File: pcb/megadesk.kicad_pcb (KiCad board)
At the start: 2 copper layers, 41.7 x 32.2 mm, 24 parts, among them J2 FFC, J3 AVR-ISP-6, J4 Interface, U1 7812, U2 HT7550-1, U3 ATtiny841-SS, U4 MCP2003B

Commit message: ignore update
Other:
- board text added: "BZ1 has no polarity"
- board text removed: "+"
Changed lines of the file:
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@@
   (gr_line (start 140.45 114.1) (end 97.7 114.1)
     (stroke (width 0.2) (type solid)) (layer "Dwgs.User"))
+  (gr_line (start 135.3 117.2) (end 133.7 118.8)
+    (stroke (width 0.3) (type default)) (layer "Cmts.User"))
+  (gr_line (start 133.7 118.8) (end 147.6 118.8)
+    (stroke (width 0.3) (type default)) (layer "Cmts.User"))
+  (gr_line (start 133.7 118.8) (end 135.3 120.4)
+    (stroke (width 0.3) (type default)) (layer "Cmts.User"))
+  (gr_line (start 133.7 118.8) (end 135.3 117.2)
+    (stroke (width 0.1) (type default)) (layer "Cmts.User"))
   (gr_line (start 121.336 70.940102) (end 121.336 117.892102)
     (stroke (width 0.15) (type solid)) (layer "Eco1.User"))
@@
     (effects (font (size 0.8 0.8) (thickness 0.125)))
   )
-  (gr_text "+" (at 129.7 118.8 270) (layer "F.SilkS")
-    (effects (font (size 1 1) (thickness 0.15)))
-  )
   (gr_text "RST\nGND" (at 115.4 118.9) (layer "F.SilkS")
     (effects (font (size 0.7 0.7) (thickness 0.1)) (justify right))
@@
     (effects (font (size 1 1) (thickness 0.15)))
   )
+  (gr_text "BZ1 has no polarity" (at 142.4 118.4) (layer "Cmts.User")
+    (effects (font (size 1 1) (thickness 0.15)) (justify left bottom))
+  )
   (segment (start 105.525 123) (end 107.625 125.1) (width 0.4) (layer "F.Cu") (net 1))

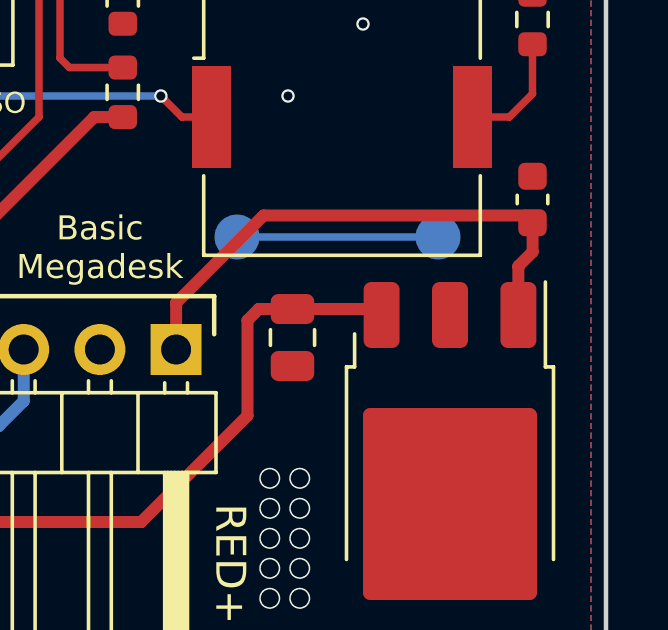
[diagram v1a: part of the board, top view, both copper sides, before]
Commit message: 2pin 7812
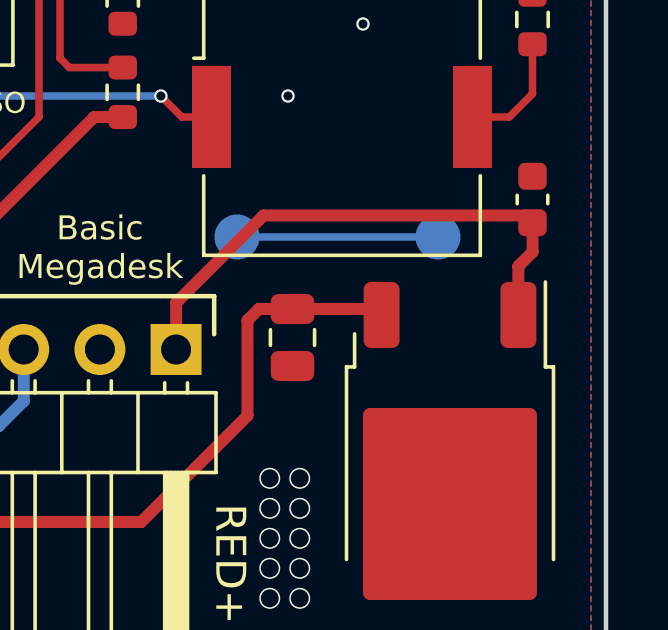
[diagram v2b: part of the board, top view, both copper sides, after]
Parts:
- U1: footprint Package_TO_SOT_SMD:TO-252-3_TabPin2 -> Package_TO_SOT_SMD:TO-252-2
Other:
- board text added: "megadesk v11a"
- board text removed: "megadesk v11"
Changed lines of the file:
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@@
     )
   )
-  (footprint "Package_TO_SOT_SMD:TO-252-3_TabPin2" (layer "F.Cu")
+  (footprint "Package_TO_SOT_SMD:TO-252-2" (layer "F.Cu")
     (at 135.7 130.44 -90)
     (descr "TO-252/DPAK SMD package, http://www.infineon.com/cms/en/product/packages/PG-TO252/PG-TO252-3-1/")
@@
     (property "ki_keywords" "Voltage Regulator 1.5A Positive")
     (attr smd)
-    (fp_text reference "U1" (at 0 -4.5 90) (layer "F.SilkS") hide
-        (effects (font (size 1 1) (thickness 0.15)))
-    )
-    (fp_text value "7812" (at 6.5 0.105 180) (layer "F.SilkS") hide
-        (effects (font (size 0.8 0.8) (thickness 0.13)))
-    )
-    (fp_text user "${REFERENCE}" (at 0 0 90) (layer "F.Fab")
+    (fp_text reference "U1" (at 0 -4.5 -90) (layer "F.SilkS") hide
+        (effects (font (size 1 1) (thickness 0.15)))
+    )
+    (fp_text value "7812" (at -4.24 -0.1 -90) (layer "F.Fab")
+        (effects (font (size 1 1) (thickness 0.15)))
+    )
+    (fp_text user "${REFERENCE}" (at 0 0 -90) (layer "F.Fab")
         (effects (font (size 1 1) (thickness 0.15)))
     )
@@
     (fp_line (start -5.81 -1.905) (end -3.11 -1.905)
       (stroke (width 0.1) (type solid)) (layer "F.Fab"))
-    (fp_line (start -5.81 -0.375) (end -5.81 0.375)
-      (stroke (width 0.1) (type solid)) (layer "F.Fab"))
-    (fp_line (start -5.81 0.375) (end -3.11 0.375)
-      (stroke (width 0.1) (type solid)) (layer "F.Fab"))
     (fp_line (start -5.81 1.905) (end -5.81 2.655)
       (stroke (width 0.1) (type solid)) (layer "F.Fab"))
@@
       (stroke (width 0.1) (type solid)) (layer "F.Fab"))
     (fp_line (start -3.11 -2.25) (end -2.11 -3.25)
-      (stroke (width 0.1) (type solid)) (layer "F.Fab"))
-    (fp_line (start -3.11 -0.375) (end -5.81 -0.375)
       (stroke (width 0.1) (type solid)) (layer "F.Fab"))
     (fp_line (start -3.11 1.905) (end -5.81 1.905)
@@
     (pad "1" smd roundrect (at -5.04 -2.28 270) (size 2.2 1.2) (layers "F.Cu" "F.Paste" "F.Mask") (roundrect_rratio 0.208333)
       (net 9 "+24V") (pinfunction "IN") (pintype "power_in"))
-    (pad "2" smd roundrect (at -5.04 0 270) (size 2.2 1.2) (layers "F.Cu" "F.Paste" "F.Mask") (roundrect_rratio 0.208333)
-      (net 2 "GND") (pinfunction "GND") (pintype "power_in"))
     (pad "2" smd roundrect (at -0.415 -1.525 270) (size 3.05 2.75) (layers "F.Cu" "F.Paste") (roundrect_rratio 0.090909)
       (net 2 "GND") (pinfunction "GND") (pintype "power_in"))
@@
     (pad "3" smd roundrect (at -5.04 2.28 270) (size 2.2 1.2) (layers "F.Cu" "F.Paste" "F.Mask") (roundrect_rratio 0.208333)
       (net 3 "+12V") (pinfunction "OUT") (pintype "power_out"))
-    (model "${KICAD6_3DMODEL_DIR}/Package_TO_SOT_SMD.3dshapes/TO-252-3_TabPin2.wrl"
+    (model "${KICAD6_3DMODEL_DIR}/Package_TO_SOT_SMD.3dshapes/TO-252-2.wrl"
       (offset (xyz 0 0 0))
       (scale (xyz 1 1 1))
@@
   (gr_line (start 99.2 136.8) (end 99.2 104.6)
     (stroke (width 0.15) (type solid)) (layer "Edge.Cuts"))
-  (gr_text "megadesk\nv11" (at 118.9 122.7) (layer "B.SilkS")
+  (gr_text "megadesk\nv11a" (at 118.9 122.7) (layer "B.SilkS")
     (effects (font (size 1.2 1.2) (thickness 0.2)) (justify mirror))
   )

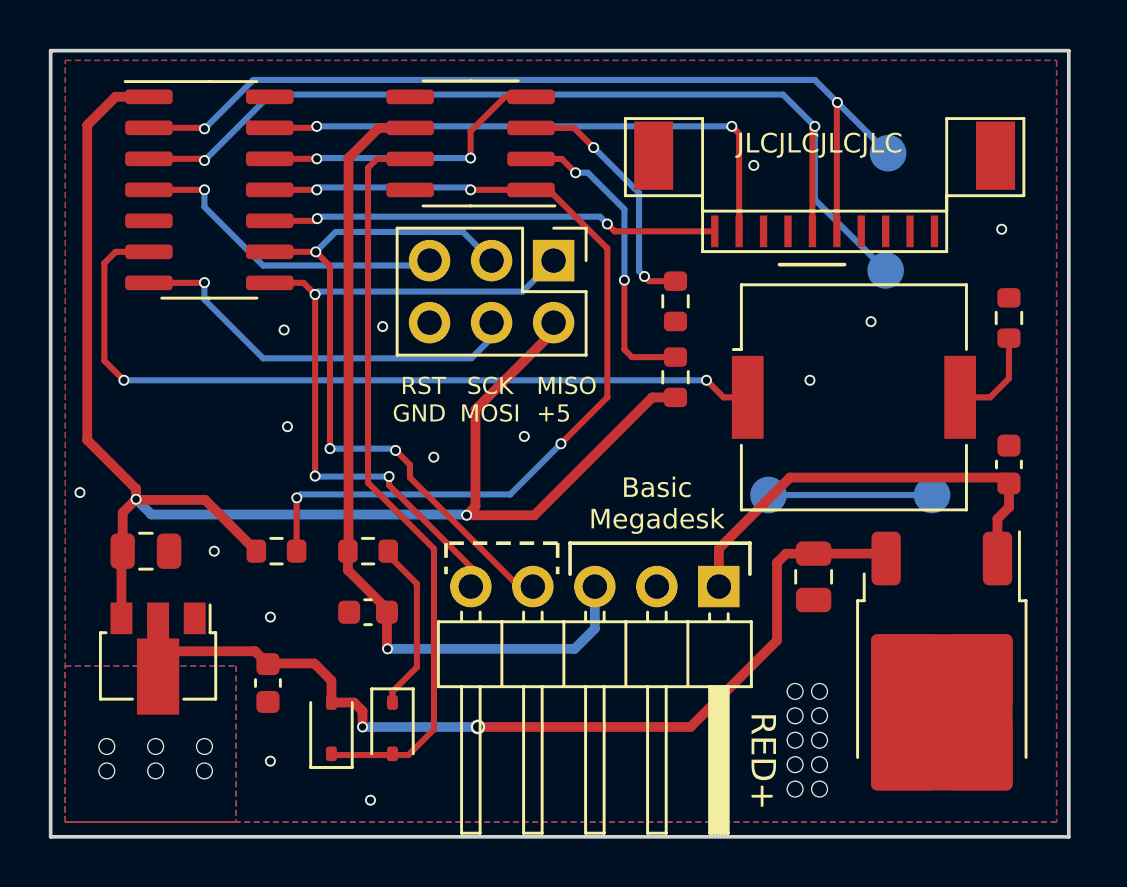
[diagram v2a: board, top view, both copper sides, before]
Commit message: FPC adjustment, 2 resistors for RP protection
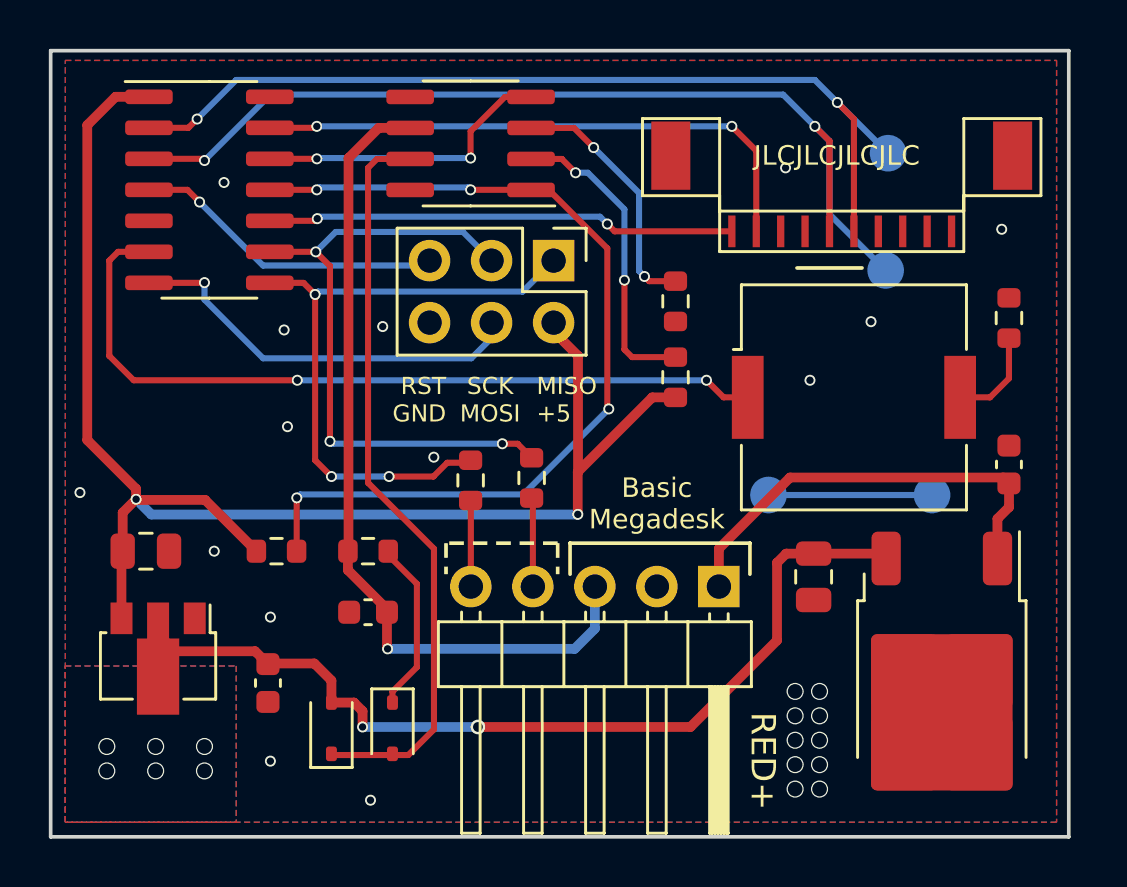
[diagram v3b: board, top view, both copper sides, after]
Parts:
- added R2: 1k, Resistor_SMD:R_0603_1608Metric, F.Cu at (118.9, 122.1)
- added R7: 1k, Resistor_SMD:R_0603_1608Metric, F.Cu at (116.4, 122.2)
- moved J2 0.70 mm to (131.6, 112.0)
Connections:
- J4 pad 4: SCK -> Net-(J4-Pin_4)
- J4 pad 5: MISO -> Net-(J4-Pin_5)
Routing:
- net Net-(J4-Pin_4): track 0.00 -> 3.65 mm
- net Net-(J4-Pin_5): track 0.00 -> 3.53 mm
- net MISO: track 28.8 -> 26.1 mm
- net SCK: track 28.6 -> 26.4 mm
- net +5V: track 63.4 -> 61.5 mm
- net B10: track 18.5 -> 19.2 mm
- net Bup: track 37.2 -> 37.9 mm
- net Bdown: track 40.0 -> 40.6 mm
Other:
- board text added: "megadesk v12"
- board text removed: "megadesk v11a"

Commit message: silkscreen change
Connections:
- net MISO renamed /MISO
- net MOSI renamed /MOSI
- net Net-(J4-Pin_4) renamed /AVRRX
- net Net-(J4-Pin_5) renamed /AVRTX
- net RST renamed /RST
- net SCK renamed /SCK
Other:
- board text added: "JLCJLCJLCJLC1"
- board text removed: "JLCJLCJLCJLC"

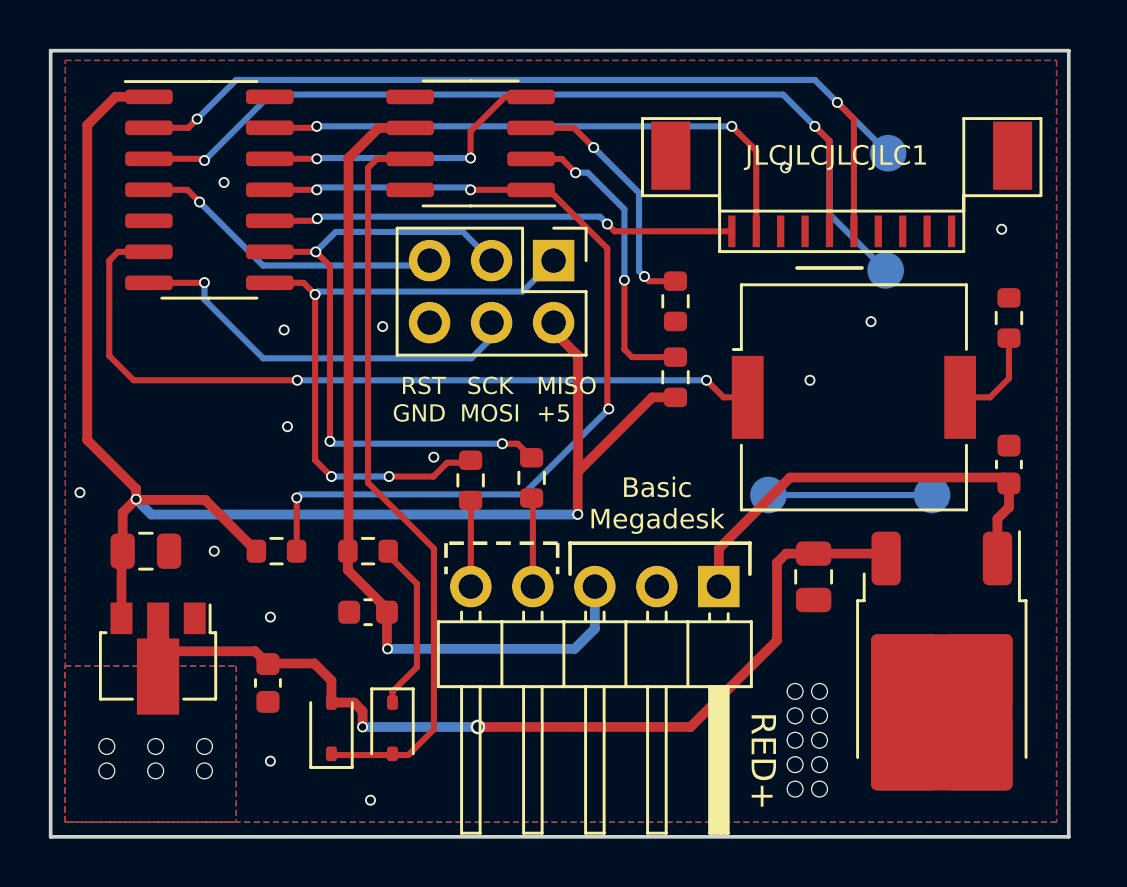
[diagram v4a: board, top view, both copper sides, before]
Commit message: Moved 5pos header to make reassembly easier, better footprint for ribbon connector compatibility, rounded PCB edges, slight increase in width (too sloppy)
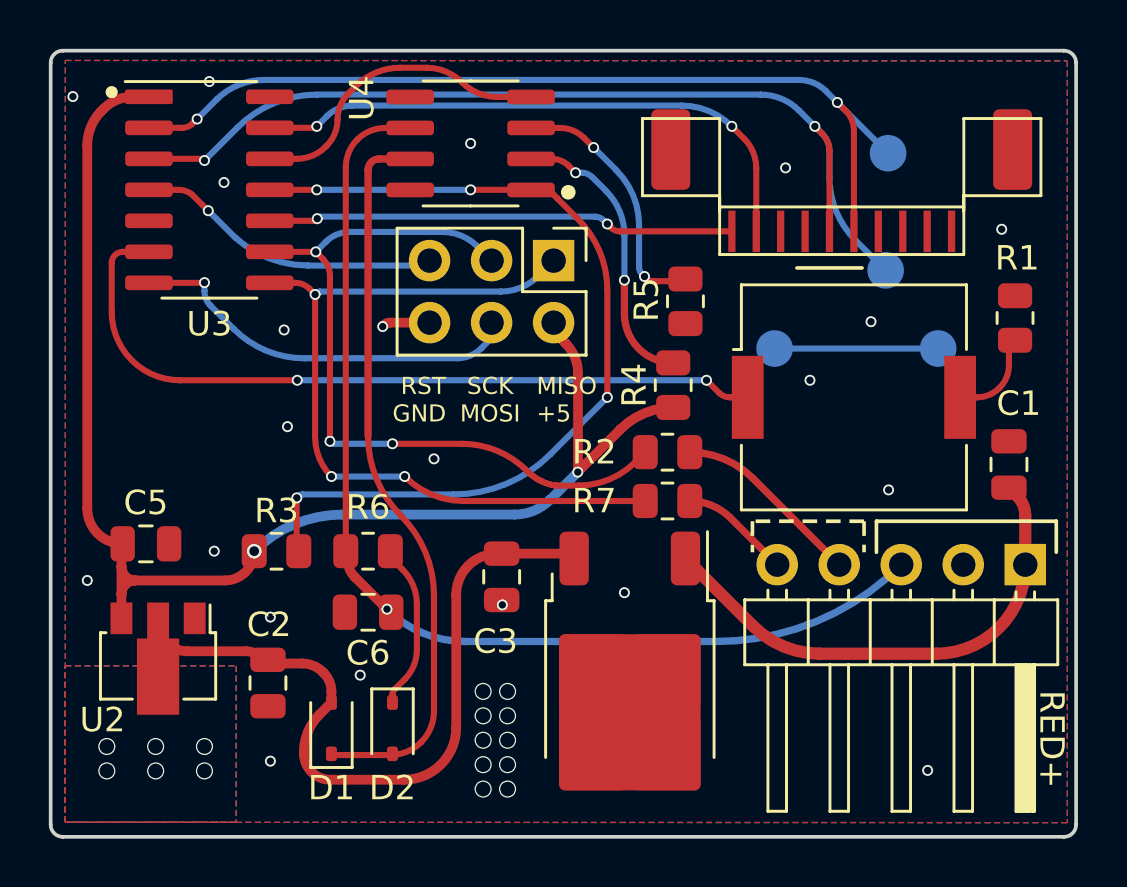
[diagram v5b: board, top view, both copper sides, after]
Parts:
- C1, C2, C6: footprint Capacitor_SMD:C_0603_1608Metric -> Capacitor_SMD:C_0805_2012Metric
- R1, R2, R3, R4, R5, R6, R7: footprint Resistor_SMD:R_0603_1608Metric -> Resistor_SMD:R_0805_2012Metric
- moved C3 12.8 mm to (117.7, 126.2)
- moved U1 12.8 mm to (122.9, 130.4)
- moved J4 12.6 mm to (139.1, 125.7)
- moved R7 8.11 mm to (124.5, 123.0), turned to 0 degrees
- moved TP1 6.01 mm to (128.8, 116.8)
- moved TP2 6.01 mm to (135.6, 116.8)
- moved R2 5.66 mm to (124.5, 121.0), turned to 0 degrees
- moved R5 0.41 mm to (125.2, 114.9)
- moved R4 0.34 mm to (124.7, 118.3)
- moved C5 0.30 mm to (103.1, 124.8)
- moved R1 0.25 mm to (138.7, 115.5)
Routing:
- net LINBUS: track 34.2 -> 44.3 mm
- net +12V: track 36.9 -> 29.6 mm, vias 8 -> 6
- net +5V: track 61.5 -> 55.2 mm
- net /MISO: track 26.1 -> 32.1 mm
- net /SCK: track 26.4 -> 31.5 mm
- net /AVRRX: track 3.65 -> 7.85 mm
- net +24V: track 17.7 -> 20.7 mm
- net GND: track 0.00 -> 1.97 mm, vias 24 -> 31
- net Net-(U3-PA2): track 38.0 -> 36.1 mm
- net /AVRTX: track 3.53 -> 4.55 mm
- net Net-(BZ1--): track 32.1 -> 31.1 mm
- net Net-(U4-CS): track 12.6 -> 13.5 mm
- net Bdown: track 40.6 -> 40.0 mm
- net Net-(U3-PA1): track 12.4 -> 12.9 mm, vias 2 -> 0
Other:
- board size 41.7 x 32.2 mm -> 42 x 32.2 mm
- rule pad_to_mask_clearance: 0.05 -> 0
- board text added: "GND"
- board text added: "LIN"
- board text added: "RX"
- board text added: "TX"
- board text removed: "Basic Megadesk"
- board text removed: "JLCJLCJLCJLC1"
